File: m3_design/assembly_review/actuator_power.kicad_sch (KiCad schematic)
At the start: 16 parts, among them Q120 AON6403, Q121 AON6403, Q122 AO3400A

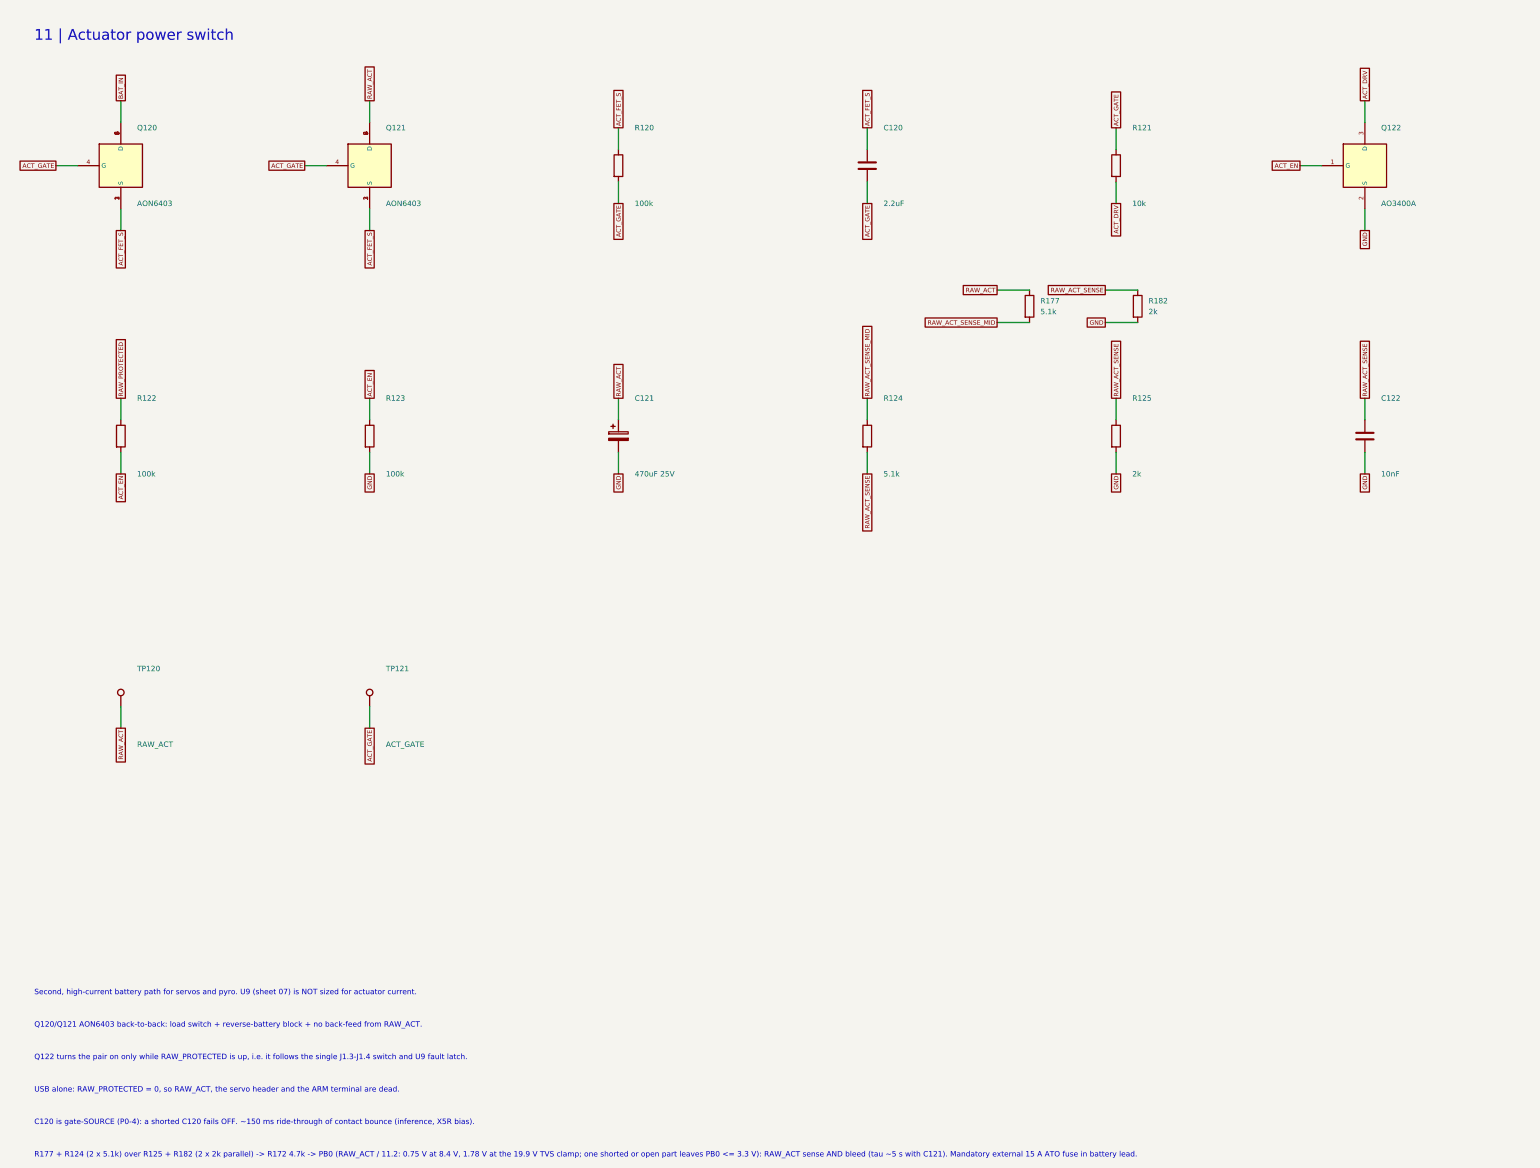
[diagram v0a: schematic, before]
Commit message: R10: m3_design/r10_build.sh and per-family stage gate; m3_design/assembly_review rebuilt as M3-ASSY-R10 (board 883d2db5..., 46 x 90 mm); tools/check.sh passes at zero; binding note bound to the board
Co-Authored-By: Claude Opus 5.5 <noreply@anthropic.com>
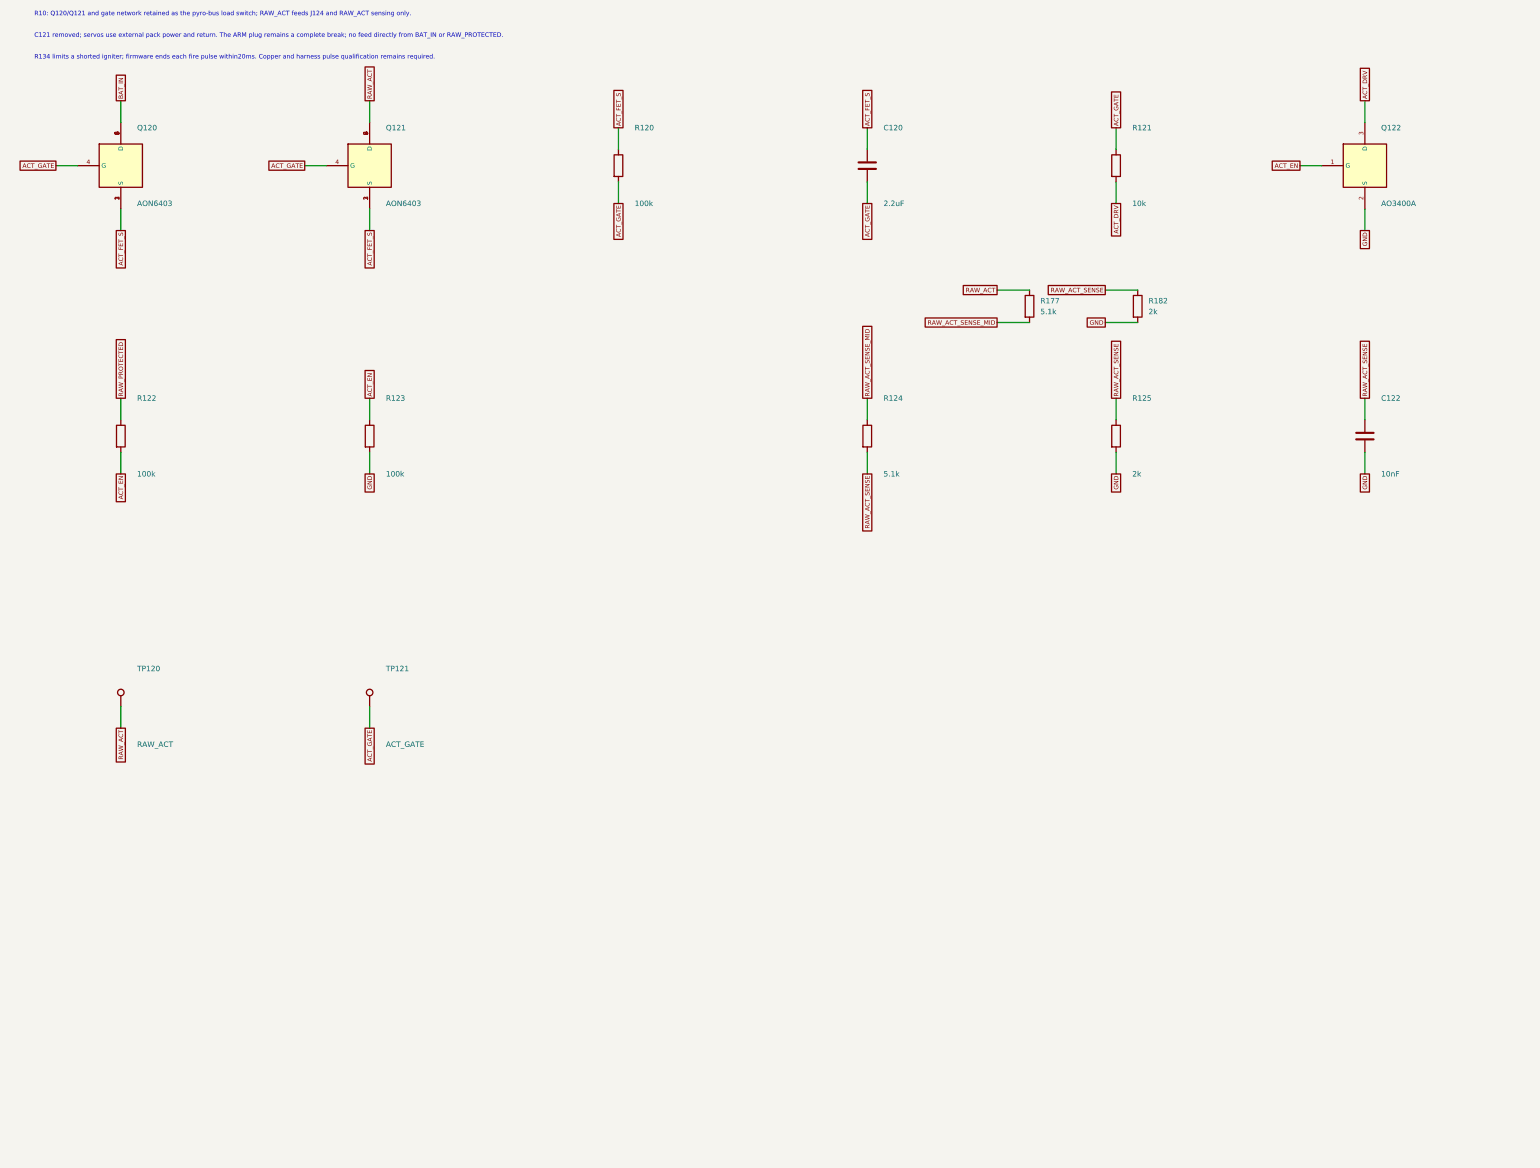
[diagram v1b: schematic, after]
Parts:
- removed C121: 470uF 25V, rocket:CAP-SMD_BD8.0-L8.3-W8.3-LS9.0-FD_H10.5, symbol M3:PolarCap
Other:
- note added: "C121 removed; servos use external pack power and return. The ARM plug remains a complete break; no feed directly from BAT_IN or RAW_PROTECTED."
- note added: "R10: Q120/Q121 and gate network retained as the pyro-bus load switch; RAW_ACT feeds J124 and RAW_ACT sensing only."
- note added: "R134 limits a shorted igniter; firmware ends each fire pulse within20ms. Copper and harness pulse qualification remains required."
- note removed: "11 | Actuator power switch"
- note removed: "C120 is gate-SOURCE (P0-4): a shorted C120 fails OFF. ~150 ms ride-through of contact bounce (inference, X5R bias)."
- note removed: "Q120/Q121 AON6403 back-to-back: load switch + reverse-battery block + no back-feed from RAW_ACT."
- note removed: "Q122 turns the pair on only while RAW_PROTECTED is up, i.e. it follows the single J1.3-J1.4 switch and U9 fault latch."
- note removed: "R177 + R124 (2 x 5.1k) over R125 + R182 (2 x 2k parallel) -> R172 4.7k -> PB0 (RAW_ACT / 11.2: 0.75 V at 8.4 V, 1.78 V at the 19.9 V TVS clamp; one shorted or open part leaves PB0 <= 3.3 V): RAW_ACT sense AND bleed (tau ~5 s with C121). Mandatory external 15 A ATO fuse in battery lead."
- note removed: "Second, high-current battery path for servos and pyro. U9 (sheet 07) is NOT sized for actuator current."
- note removed: "USB alone: RAW_PROTECTED = 0, so RAW_ACT, the servo header and the ARM terminal are dead."
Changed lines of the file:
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@@
 		(title "11 | Actuator power switch")
 		(date "2026-09-25")
-		(rev "M3-ASSY-R9")
+		(rev "M3-ASSY-R10")
 		(company "Single-board M3 candidate; actuator merge, not bench-verified"))
 	(symbol
@@
 )
 	(symbol
-		(lib_id "M3:PolarCap")
-		(at 157.48 114.3 0)
-		(unit 1)
-		(in_bom yes)
-		(on_board yes)
-		(dnp no)
-		(property "Reference" "C121"
-			(at 161.29 105.41 0)
-			(effects
-				(font
-					(size 1.27 1.27))
-				(justify left)))
-		(property "Value" "470uF 25V"
-			(at 161.29 123.19 0)
-			(effects
-				(font
-					(size 1.27 1.27))
-				(justify left)))
-		(property "Footprint" "rocket:CAP-SMD_BD8.0-L8.3-W8.3-LS9.0-FD_H10.5"
-			(at 157.48 114.3 0)
-			(hide yes)
-			(effects
-				(font
-					(size 1.27 1.27))))
-		(property "Datasheet" ""
-			(at 157.48 114.3 0)
-			(hide yes)
-			(effects
-				(font
-					(size 1.27 1.27))))
-		(property "LCSC" "C46550466"
-			(at 157.48 114.3 0)
-			(hide yes)
-			(effects
-				(font
-					(size 1.27 1.27))))
-		(property "Manufacturer" "JIERR"
-			(at 157.48 114.3 0)
-			(hide yes)
-			(effects
-				(font
-					(size 1.27 1.27))))
-		(property "Manufacturer Part" "MA25V470M8x10"
-			(at 157.48 114.3 0)
-			(hide yes)
-			(effects
-				(font
-					(size 1.27 1.27))))
-		(instances
-			(project "m3"
-				(path "/6007a7db-6a58-5660-8beb-956dea045ff8/6133d301-6422-5dca-9dda-573ff465fb31"
-					(reference "C121")
-					(unit 1)))))
-	(wire
-		(pts
-			(xy 157.48 110.49)
-			(xy 157.48 105.41))
-		(stroke
-			(width 0)
-			(type default))
-)
-	(global_label "RAW_ACT"
-		(shape passive)
-		(at 157.48 105.41 90)
-		(effects
-			(font
-				(size 1.05 1.05))
-			(justify left))
-)
-	(wire
-		(pts
-			(xy 157.48 118.11)
-			(xy 157.48 123.19))
-		(stroke
-			(width 0)
-			(type default))
-)
-	(global_label "GND"
-		(shape passive)
-		(at 157.48 123.19 270)
-		(effects
-			(font
-				(size 1.05 1.05))
-			(justify right))
-)
-	(symbol
 		(lib_id "M3:R")
 		(at 215.9 114.3 0)
@@
 			(justify right))
 )
-	(text "11 | Actuator power switch"
-		(at 20.32 20.32 0)
-		(effects
-			(font
-				(size 2.54 2.54))
-			(justify left))
-)
-	(text "Second, high-current battery path for servos and pyro. U9 (sheet 07) is NOT sized for actuator current."
-		(at 20.32 245 0)
-		(effects
-			(font
-				(size 1.27 1.27))
-			(justify left))
-)
-	(text "Q120/Q121 AON6403 back-to-back: load switch + reverse-battery block + no back-feed from RAW_ACT."
-		(at 20.32 252.62 0)
-		(effects
-			(font
-				(size 1.27 1.27))
-			(justify left))
-)
-	(text "Q122 turns the pair on only while RAW_PROTECTED is up, i.e. it follows the single J1.3-J1.4 switch and U9 fault latch."
-		(at 20.32 260.24 0)
-		(effects
-			(font
-				(size 1.27 1.27))
-			(justify left))
-)
-	(text "USB alone: RAW_PROTECTED = 0, so RAW_ACT, the servo header and the ARM terminal are dead."
-		(at 20.32 267.86 0)
-		(effects
-			(font
-				(size 1.27 1.27))
-			(justify left))
-)
-	(text "C120 is gate-SOURCE (P0-4): a shorted C120 fails OFF. ~150 ms ride-through of contact bounce (inference, X5R bias)."
-		(at 20.32 275.48 0)
-		(effects
-			(font
-				(size 1.27 1.27))
-			(justify left))
-)
-	(text "R177 + R124 (2 x 5.1k) over R125 + R182 (2 x 2k parallel) -> R172 4.7k -> PB0 (RAW_ACT / 11.2: 0.75 V at 8.4 V, 1.78 V at the 19.9 V TVS clamp; one shorted or open part leaves PB0 <= 3.3 V): RAW_ACT sense AND bleed (tau ~5 s with C121). Mandatory external 15 A ATO fuse in battery lead."
-		(at 20.32 283.1 0)
-		(effects
-			(font
-				(size 1.27 1.27))
-			(justify left))
-)
 	(symbol
 		(lib_id "M3:R")
@@
 			(justify right))
 )
+	(text "R10: Q120/Q121 and gate network retained as the pyro-bus load switch; RAW_ACT feeds J124 and RAW_ACT sensing only."
+		(at 20.32 15.24 0)
+		(effects
+			(font
+				(size 1.05 1.05))
+			(justify left))
+)
+	(text "C121 removed; servos use external pack power and return. The ARM plug remains a complete break; no feed directly from BAT_IN or RAW_PROTECTED."
+		(at 20.32 20.32 0)
+		(effects
+			(font
+				(size 1.05 1.05))
+			(justify left))
+)
+	(text "R134 limits a shorted igniter; firmware ends each fire pulse within20ms. Copper and harness pulse qualification remains required."
+		(at 20.32 25.4 0)
+		(effects
+			(font
+				(size 1.05 1.05))
+			(justify left))
+)
 	(sheet_instances
